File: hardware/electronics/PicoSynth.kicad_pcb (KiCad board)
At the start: 2 copper layers, 102 parts, among them J1 Conn_01x06_Socket, SW1 RotaryEncoder_Switch_MP, SW10 SW_Push_45deg, SW11 SW_Push_45deg, SW12 SW_Push_45deg, SW13 SW_Push_45deg, SW14 SW_Push_45deg, SW15 SW_Push_45deg, SW16 SW_Push_45deg, SW17 SW_Push_45deg, SW18 SW_Push_45deg, SW19 SW_Push_45deg, SW2 RotaryEncoder_Switch_MP, SW20 SW_Push_45deg, SW3 RotaryEncoder_Switch_MP, SW4 RotaryEncoder_Switch_MP, SW5 SW_Push_45deg, SW6 SW_Push_45deg, SW7 SW_Push_45deg, SW8 SW_Push_45deg, SW9 SW_Push_45deg, U1 Pico, U5 PCF8574, U6 PCF8574, U7 PCF8574

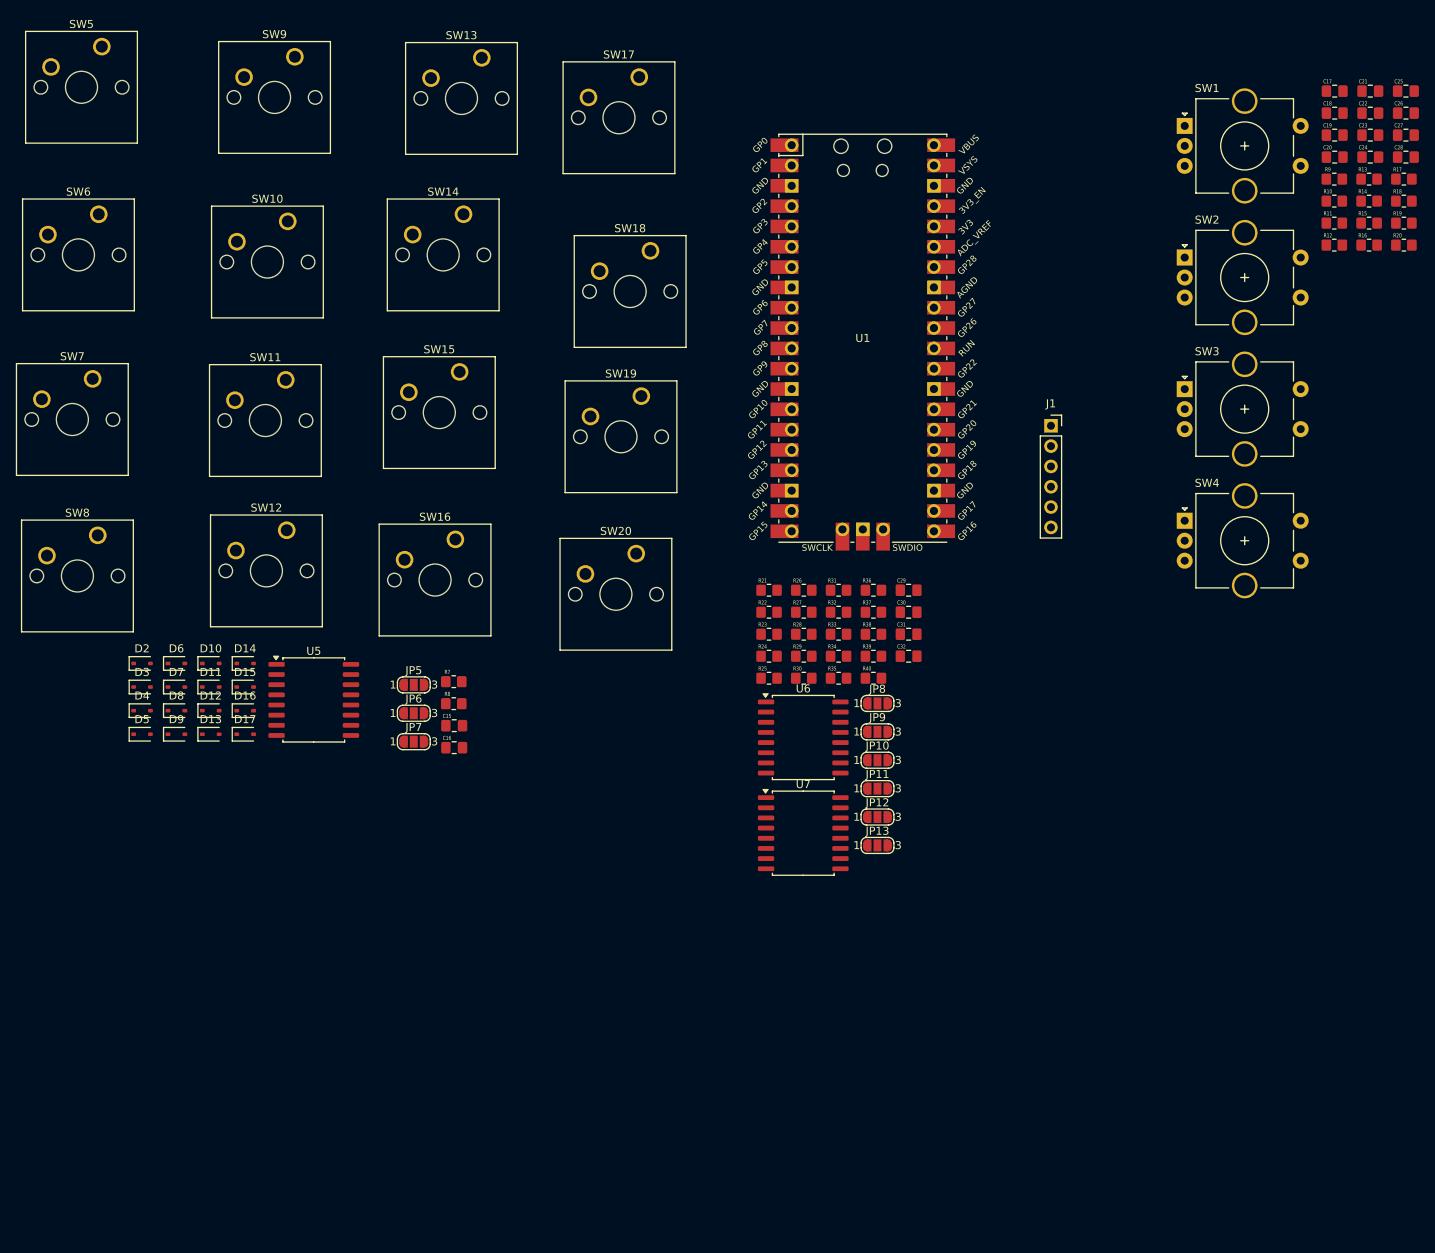
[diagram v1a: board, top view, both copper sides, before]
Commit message: SD card and i2c for display added, starting some component placement
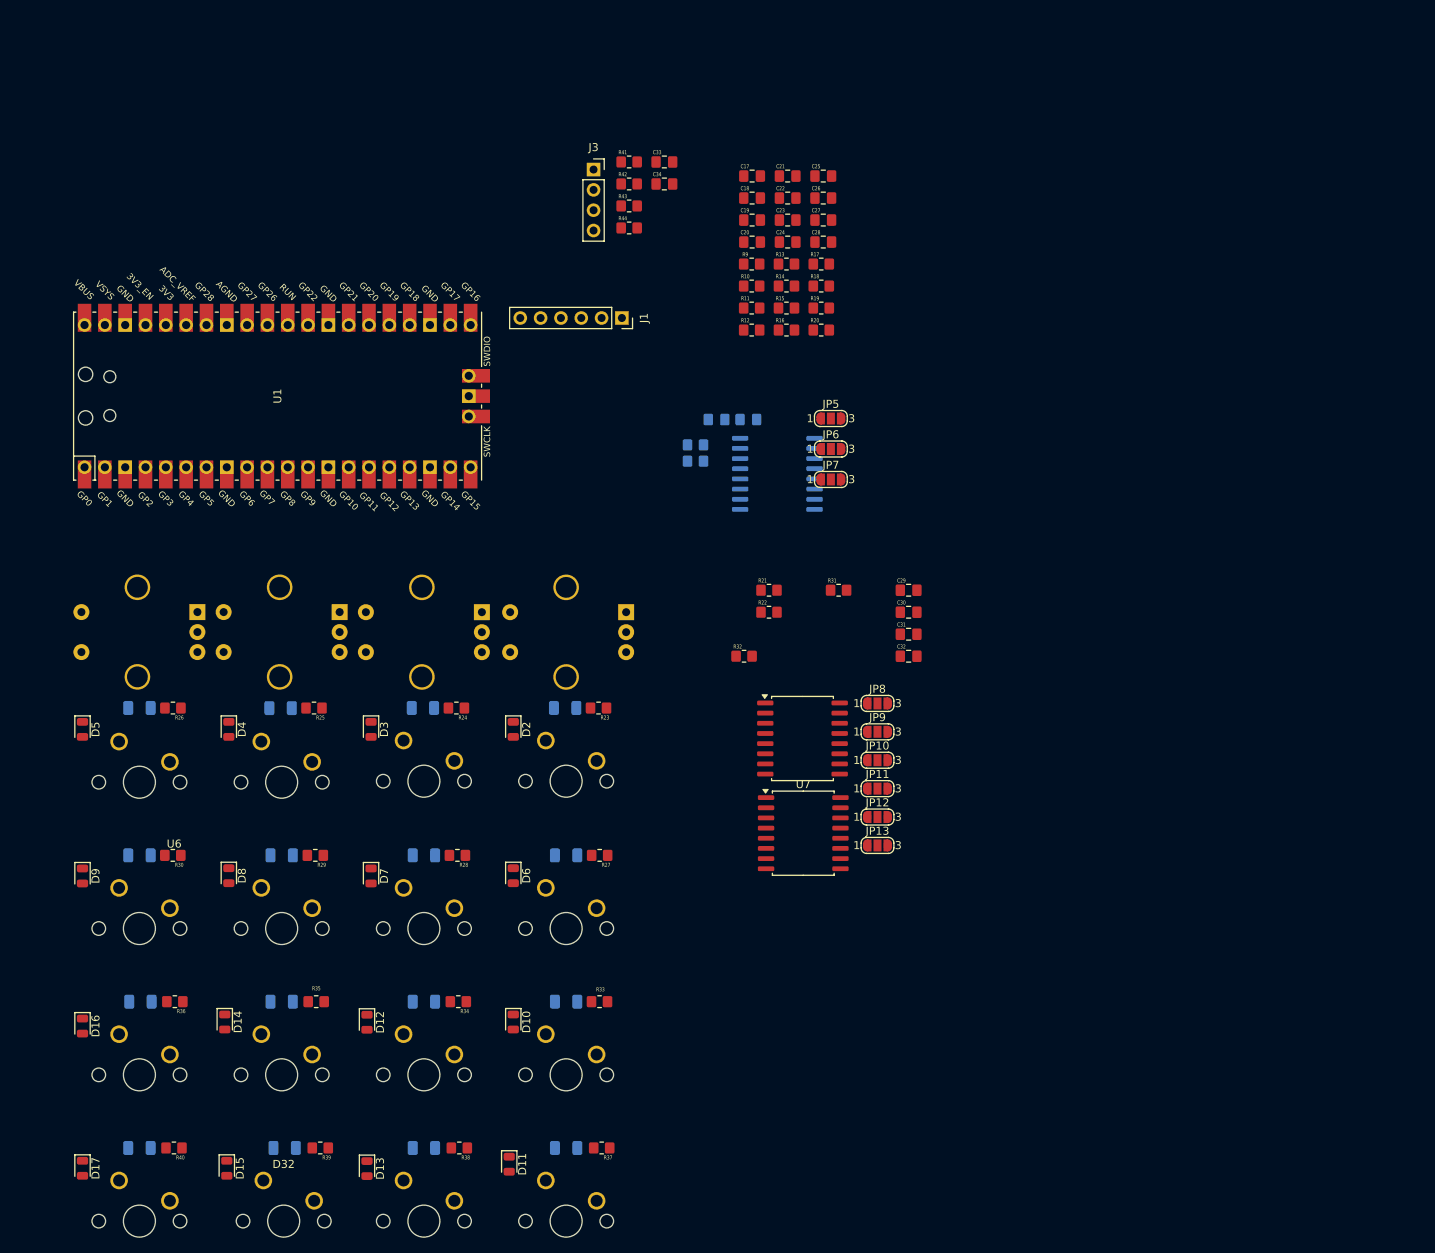
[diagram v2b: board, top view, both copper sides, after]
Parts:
- added C33: 2.2uF, Cern_Ignition:C_0805_2012Metric_Pad1.18x1.45mm_HandSolder_modif, F.Cu at (108.8, 39.3)
- added C34: 100nF, Cern_Ignition:C_0805_2012Metric_Pad1.18x1.45mm_HandSolder_modif, F.Cu at (108.8, 42.1)
- added D18: LED, LED_SMD:LED_1206_3216Metric, B.Cu at (96.4, 107.6)
- added D19: LED, LED_SMD:LED_1206_3216Metric, B.Cu at (78.6, 107.6)
- added D20: LED, LED_SMD:LED_1206_3216Metric, B.Cu at (60.8, 107.6)
- added D21: LED, LED_SMD:LED_1206_3216Metric, B.Cu at (43.2, 107.6)
- added D22: LED, LED_SMD:LED_1206_3216Metric, B.Cu at (96.5, 126.0)
- added D23: LED, LED_SMD:LED_1206_3216Metric, B.Cu at (78.7, 126.0)
- added D24: LED, LED_SMD:LED_1206_3216Metric, B.Cu at (61.0, 126.0)
- added D25: LED, LED_SMD:LED_1206_3216Metric, B.Cu at (43.2, 126.0)
- added D26: LED, LED_SMD:LED_1206_3216Metric, B.Cu at (96.5, 144.3)
- added D27: LED, LED_SMD:LED_1206_3216Metric, B.Cu at (78.7, 144.3)
- added D28: LED, LED_SMD:LED_1206_3216Metric, B.Cu at (61.0, 144.3)
- added D29: LED, LED_SMD:LED_1206_3216Metric, B.Cu at (43.3, 144.3)
- added D30: LED, LED_SMD:LED_1206_3216Metric, B.Cu at (96.5, 162.6)
- added D31: LED, LED_SMD:LED_1206_3216Metric, B.Cu at (78.7, 162.6)
- added D32: LED, LED_SMD:LED_1206_3216Metric, B.Cu at (61.3, 162.6)
- added D33: LED, LED_SMD:LED_1206_3216Metric, B.Cu at (43.2, 162.6)
- added J3: Conn_01x04_Socket, Connector_PinSocket_2.54mm:PinSocket_1x04_P2.54mm_Vertical, F.Cu at (99.9, 40.3)
- added R41: 10k, Cern_Ignition:R_0805_2012Metric_Pad1.20x1.40mm_HandSolder_modif, F.Cu at (104.4, 39.3)
- added R42: 10k, Cern_Ignition:R_0805_2012Metric_Pad1.20x1.40mm_HandSolder_modif, F.Cu at (104.4, 42.1)
- added R43: 10k, Cern_Ignition:R_0805_2012Metric_Pad1.20x1.40mm_HandSolder_modif, F.Cu at (104.4, 44.8)
- added R44: 10k, Cern_Ignition:R_0805_2012Metric_Pad1.20x1.40mm_HandSolder_modif, F.Cu at (104.4, 47.6)
- C15, C16, R7, R8, SW1, SW2, SW3, SW4, U5: moved to B.Cu
- D10, D11, D12, D13, D14, D15, D16, D17, D2, D3, D4, D5, D6, D7, D8, D9: footprint Diode_SMD:D_SOD-323 -> Diode_SMD:D_0805_2012Metric
- JP10, JP13, JP7: value FLT_Jumper -> A2_Jumper
- JP11, JP5, JP8: value FLT_Jumper -> A0_Jumper
- JP12, JP6, JP9: value FLT_Jumper -> A1_Jumper
- SW10, SW11, SW12, SW13, SW14, SW15, SW16, SW17, SW18, SW19, SW20, SW5, SW6, SW7, SW8, SW9: footprint Lame_Lib:SW_Cherry_MX_1.00u_PCB -> Cherry_MX_switches:Cherry-MX_PCB-Mounted; moved to B.Cu
- moved SW17 132.5 mm to (61.0, 153.4), turned to 180 degrees
- moved SW18 129.7 mm to (61.2, 171.7), turned to 180 degrees
- moved SW13 127.6 mm to (96.5, 153.4), turned to 180 degrees
- moved SW14 126.5 mm to (96.5, 171.7), turned to 180 degrees
- moved SW4 123.9 mm to (50.4, 95.6), turned to 180 degrees
- moved SW9 114.1 mm to (96.5, 135.1), turned to 180 degrees
- moved SW3 109.2 mm to (68.2, 95.6), turned to 180 degrees
- moved SW5 108.6 mm to (96.5, 116.7), turned to 180 degrees
- moved SW19 105.5 mm to (43.2, 153.4), turned to 180 degrees
- moved R40 105.3 mm to (47.5, 162.6), turned to 180 degrees
- moved SW20 104.0 mm to (43.2, 171.7), turned to 180 degrees
- moved R36 101.3 mm to (47.6, 144.3), turned to 180 degrees
- moved SW2 98.4 mm to (86.0, 95.6), turned to 180 degrees
- moved SW1 92.6 mm to (104.0, 95.6), turned to 180 degrees
- moved R39 92.5 mm to (65.8, 162.6), turned to 180 degrees
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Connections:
- U1 pad 10: unconnected-(U1-GPIO7-Pad10) -> /Encoder0_B
- U1 pad 11: unconnected-(U1-GPIO8-Pad11) -> /Encoder0_Sw
- U1 pad 12: unconnected-(U1-GPIO9-Pad12) -> /Encoder1_Sw
- U1 pad 14: unconnected-(U1-GPIO10-Pad14) -> /Encoder1_A
- U1 pad 15: unconnected-(U1-GPIO11-Pad15) -> /Encoder1_B
- U1 pad 25: unconnected-(U1-GPIO19-Pad25) -> /Encoder2_Sw
- U1 pad 26: unconnected-(U1-GPIO20-Pad26) -> /Encoder2_B
- U1 pad 27: unconnected-(U1-GPIO21-Pad27) -> /Encoder2_A
- U1 pad 29: unconnected-(U1-GPIO22-Pad29) -> /Encoder3_Sw
- U1 pad 30: unconnected-(U1-RUN-Pad30) -> /Encoder3_B
- U1 pad 31: unconnected-(U1-GPIO26_ADC0-Pad31) -> /Encoder3_A
- U1 pad 4: unconnected-(U1-GPIO2-Pad4) -> /CLK
- U1 pad 5: unconnected-(U1-GPIO3-Pad5) -> /CMD
- U1 pad 6: unconnected-(U1-GPIO4-Pad6) -> /DAT0
- U1 pad 7: unconnected-(U1-GPIO5-Pad7) -> /CD
- U1 pad 9: unconnected-(U1-GPIO6-Pad9) -> /Encoder0_A

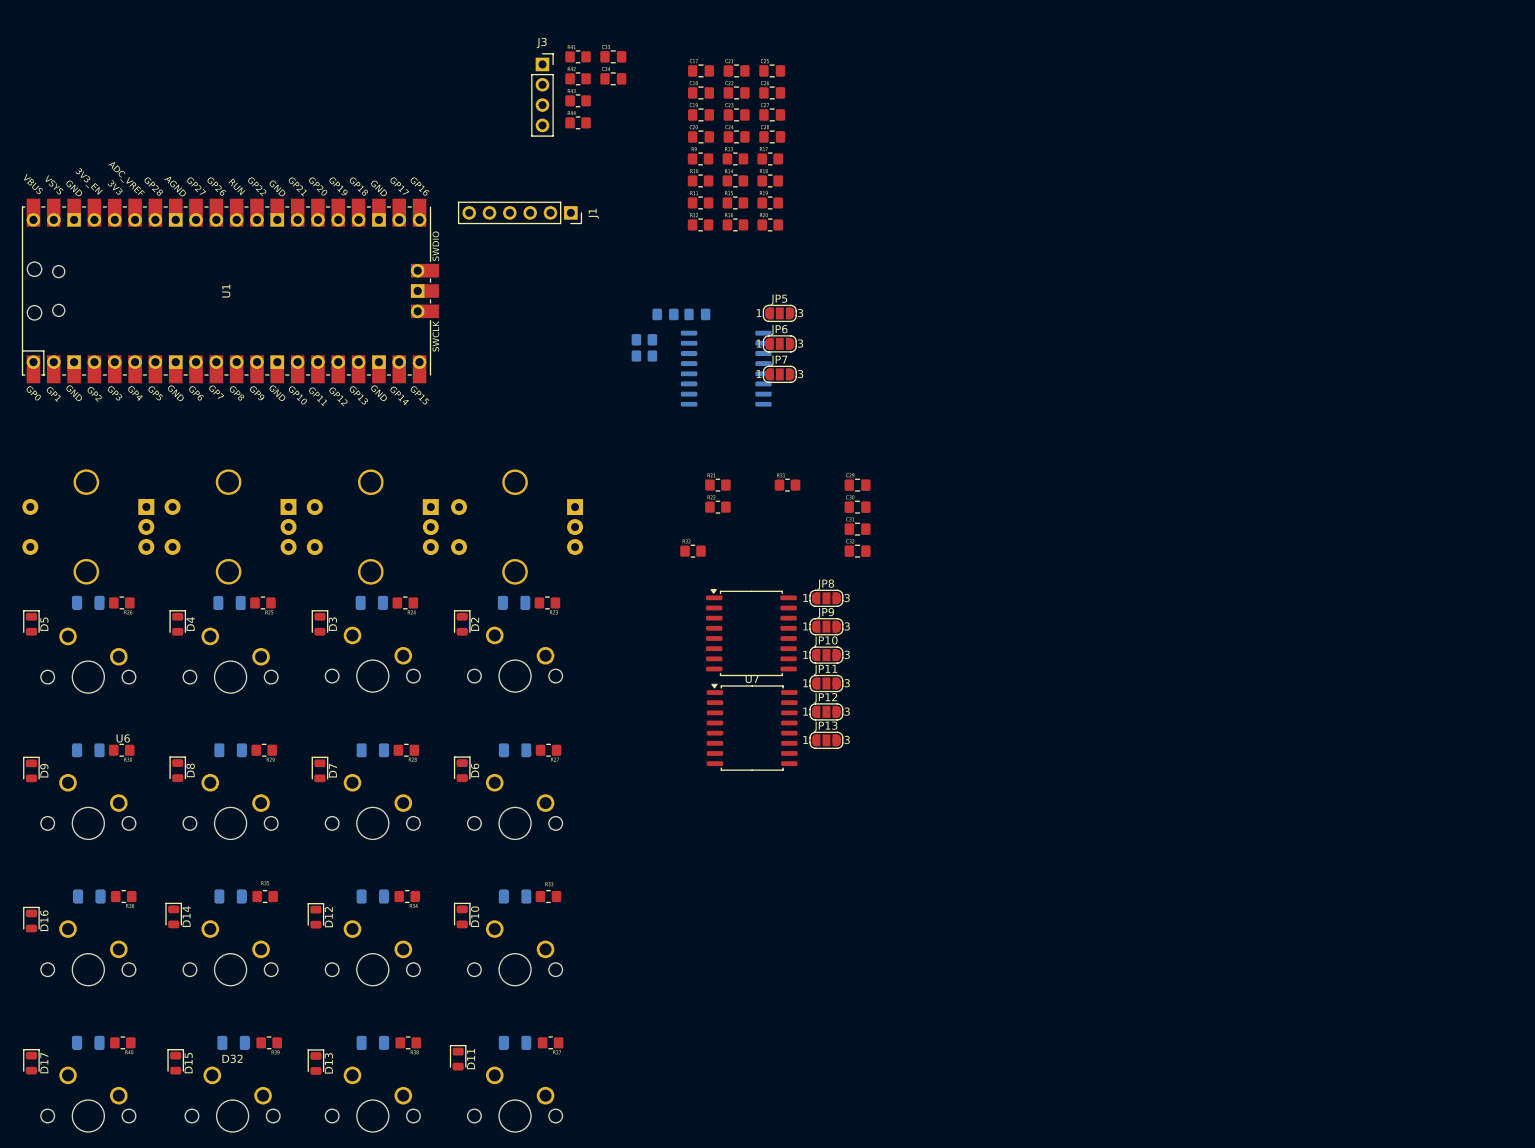
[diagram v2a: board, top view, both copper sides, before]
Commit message: New horizontal layout
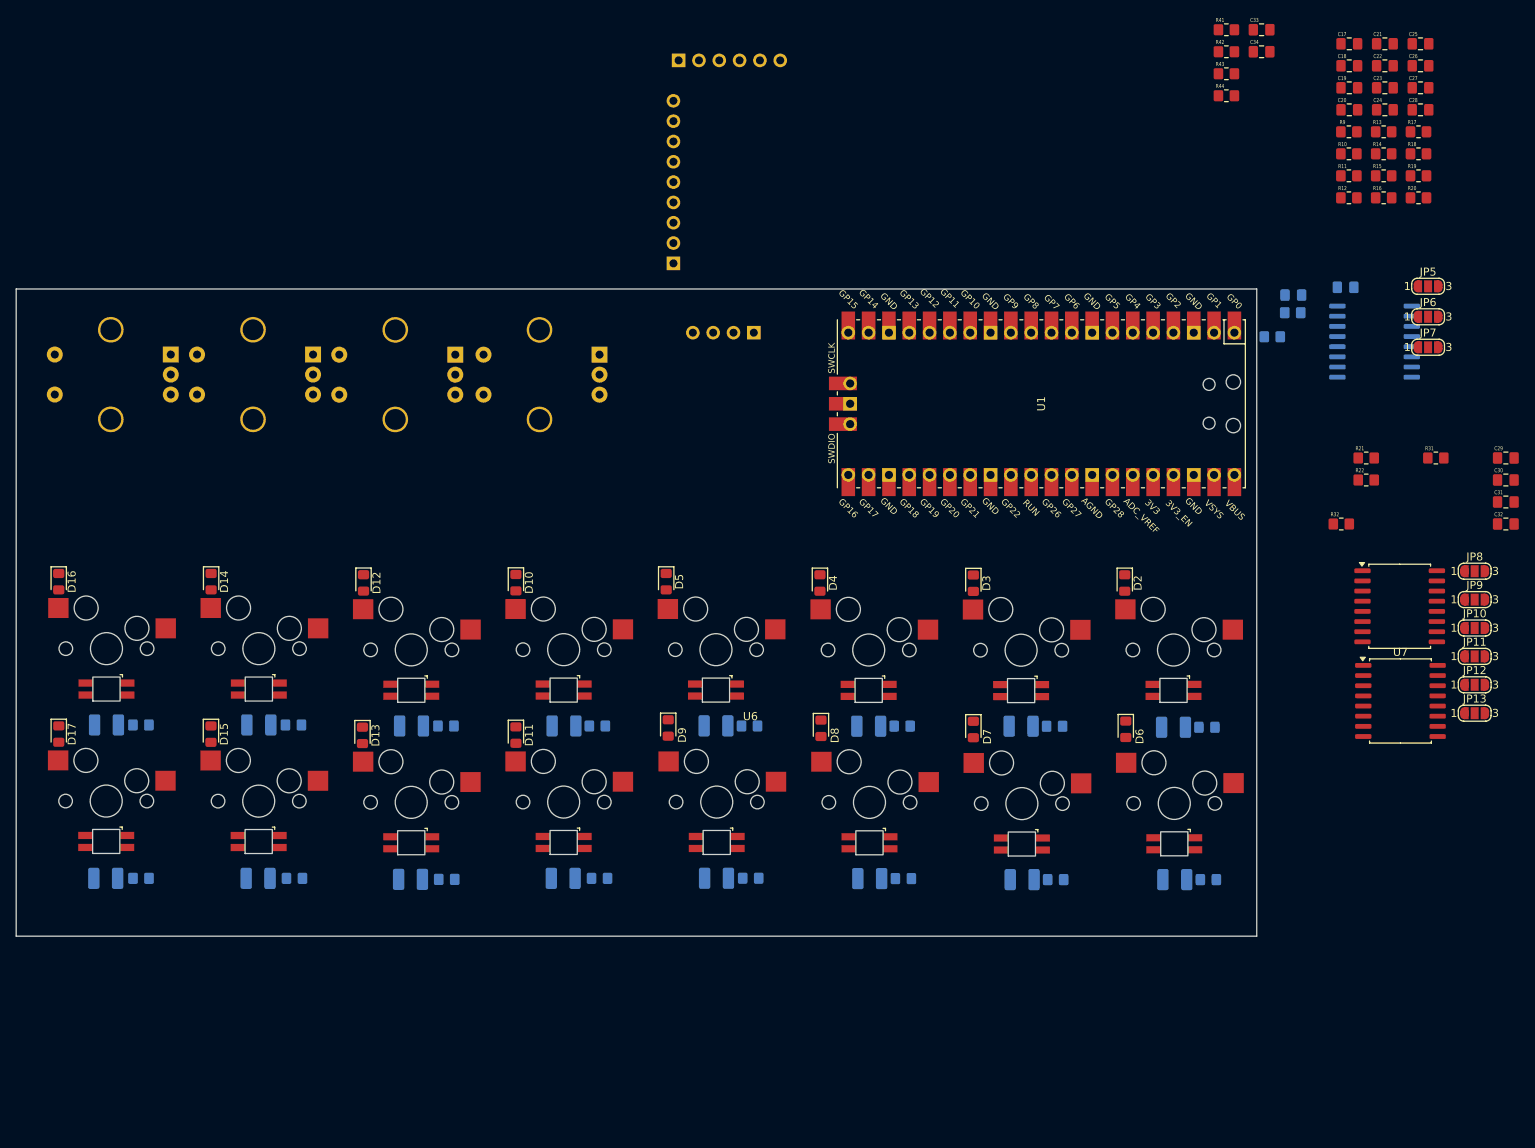
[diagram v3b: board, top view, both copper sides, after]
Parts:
- added J4: Conn_01x09_Socket, Connector_PinSocket_2.54mm:PinSocket_1x09_P2.54mm_Vertical, B.Cu at (116.3, 65.1)
- D10, D11, D12, D13, D14, D15, D16, D17, D2, D3, D4, D5, D6, D7, D8, D9: footprint Diode_SMD:D_0805_2012Metric -> Diode_SMD:D_0805_2012Metric_Pad1.15x1.40mm_HandSolder
- D18, D19, D20, D21, D22, D23, D24, D25, D26, D27, D28, D29, D30, D31, D32, D33: footprint LED_SMD:LED_1206_3216Metric -> LED_SMD:LED_1210_3225Metric_Pad1.42x2.65mm_HandSolder
- J1, J3, R23, R24, R25, R26, R27, R28, R29, R30, R33, R34, R35, R36, R37, R38, R39, R40: moved to B.Cu
- SW1, SW2, SW3, SW4: footprint Rotary_Encoder:RotaryEncoder_Alps_EC11E-Switch_Vertical_H20mm_CircularMountingHoles -> Lame_Lib:RotaryEncoder_Alps_EC11E-Switch_Vertical_H20mm_CircularMountingHoles
- SW10, SW11, SW12, SW13, SW14, SW15, SW16, SW17, SW18, SW19, SW20, SW5, SW6, SW7, SW8, SW9: footprint Cherry_MX_switches:Cherry-MX_PCB-Mounted -> Cherry_MX_switches:Cherry-MX_PCB-Mounted_LTST-A683CEGBW_Kailh_Socket
- moved U1 102.8 mm to (162.3, 82.7), turned to -90 degrees
- moved D22 84.0 mm to (179.0, 142.2)
- moved R27 84.0 mm to (183.2, 142.2)
- moved D18 83.9 mm to (178.8, 123.1)
- moved R23 83.9 mm to (183.0, 123.1)
- moved D6 83.1 mm to (172.9, 123.4)
- moved D2 83.0 mm to (172.7, 105.1)
- moved D23 82.8 mm to (159.9, 142.2)
- moved R28 82.8 mm to (164.1, 142.2)
- moved R24 82.6 mm to (164.0, 123.0)
- moved D19 82.6 mm to (159.8, 123.0)
- moved SW9 82.4 mm to (178.9, 132.6)
- moved SW5 82.4 mm to (178.8, 113.5)
- moved D7 81.8 mm to (153.8, 123.4)
- moved D3 81.8 mm to (153.8, 105.1)
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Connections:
- J1 pad 1: /+5V -> GND
- J1 pad 2: GND -> /BCK
- J1 pad 3: /LRCK -> /DIN
- J1 pad 4: /DIN -> /LRCK
- J1 pad 5: /BCK -> GND
- J1 pad 6: GND -> /+5V
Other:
- board outline added: 155.1 x 80.9 mm
